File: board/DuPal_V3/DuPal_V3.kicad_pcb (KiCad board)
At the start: 2 copper layers, 116.8 x 73.7 mm, 129 parts, among them J1 ZIF Socket, J2 Debug Header, J3 Extra, K1 G6K-2, Q1 2N3904, SW1 RESET, U1 Pico, U10 74HCT166, U11 74HCT166, U12 74HCT166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

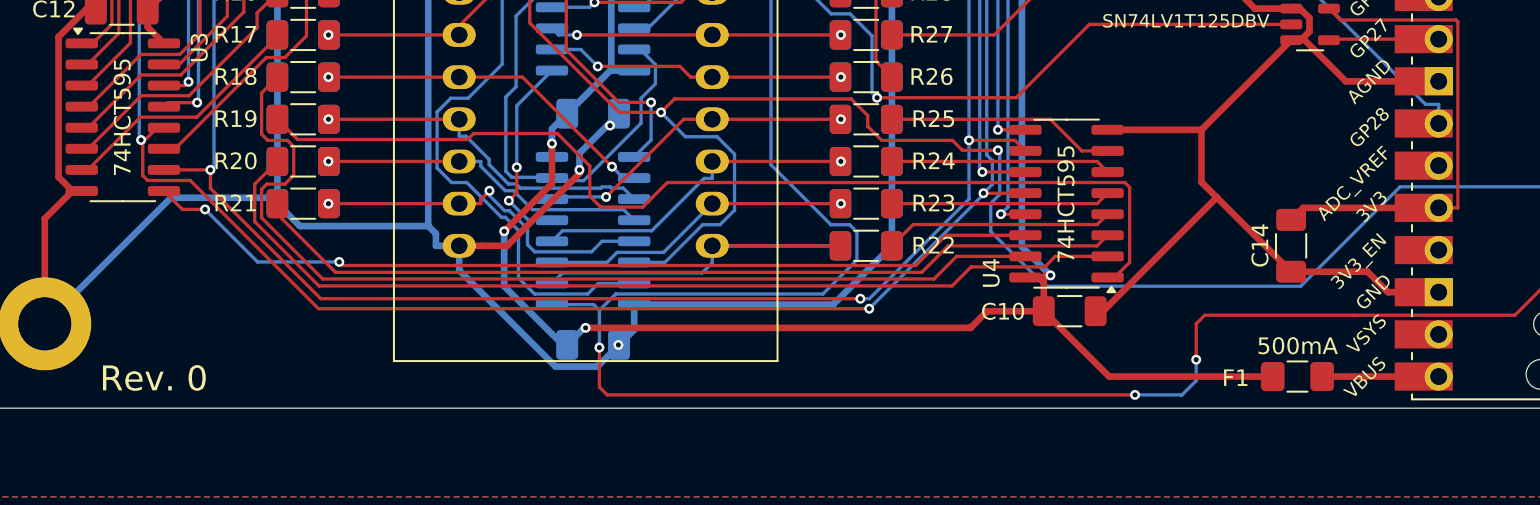
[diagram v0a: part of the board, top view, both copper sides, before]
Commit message: Add external pullup on /RELAY_ENABLE pin to avoid triggering at powerup
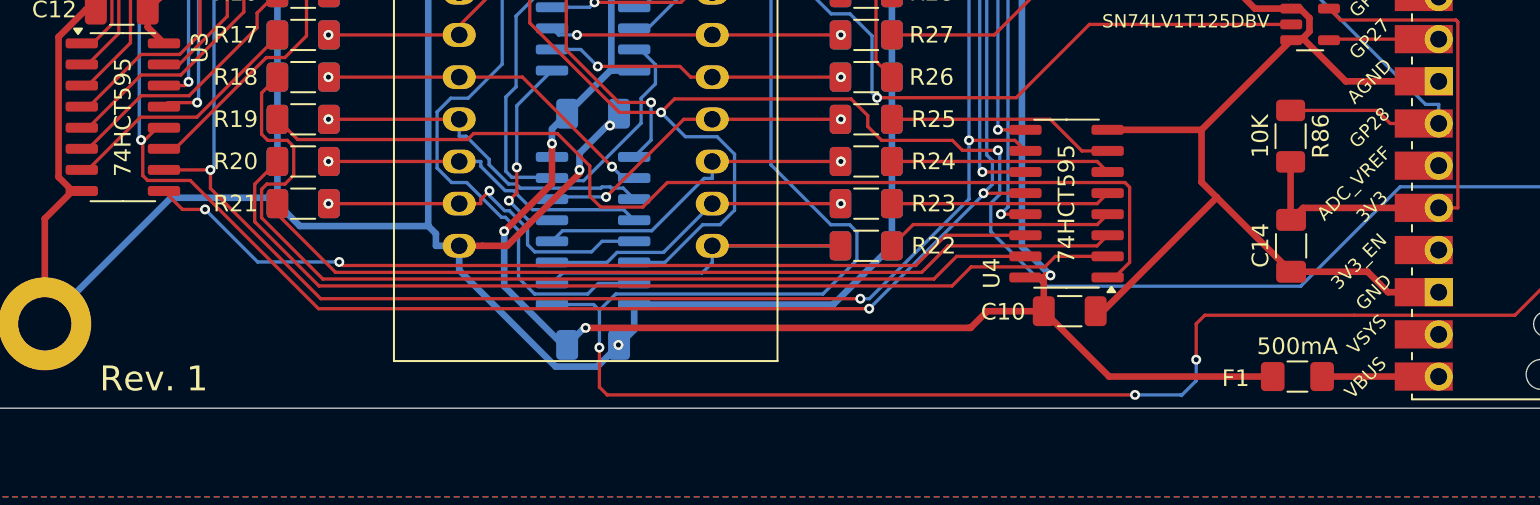
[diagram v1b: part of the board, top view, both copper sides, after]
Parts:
- added R86: 10K, Resistor_SMD:R_1206_3216Metric_Pad1.30x1.75mm_HandSolder, F.Cu at (172.3, 97.9)
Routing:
- net /~{RELAY_ENABLE}: track 46.1 -> 55.4 mm
- net +3V3: track 29.6 -> 33.1 mm
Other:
- board text added: "Rev. 1"
- board text removed: "Rev. 0"
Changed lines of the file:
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@@
 	(footprint "Resistor_SMD:R_1206_3216Metric_Pad1.30x1.75mm_HandSolder"
 		(layer "F.Cu")
+		(at 172.309 97.917 -90)
+		(descr "Resistor SMD 1206 (3216 Metric), square (rectangular) end terminal, IPC_7351 nominal with elongated pad for handsoldering. (Body size source: IPC-SM-782 page 72, https://www.pcb-3d.com/wordpress/wp-content/uploads/ipc-sm-782a_amendment_1_and_2.pdf), generated with kicad-footprint-generator")
+		(tags "resistor handsolder")
+		(property "Reference" "R86"
+			(at 0 -1.82 90)
+			(layer "F.SilkS")
+			(effects
+				(font
+					(size 1 1)
+					(thickness 0.15)
+				)
+			)
+		)
+		(property "Value" "10K"
+			(at 0 1.82 90)
+			(layer "F.SilkS")
+			(effects
+				(font
+					(size 1 1)
+					(thickness 0.15)
+				)
+			)
+		)
+		(property "Footprint" "Resistor_SMD:R_1206_3216Metric_Pad1.30x1.75mm_HandSolder"
+			(at 0 0 -90)
+			(unlocked yes)
+			(layer "F.Fab")
+			(hide yes)
+			(effects
+				(font
+					(size 1.27 1.27)
+					(thickness 0.15)
+				)
+			)
+		)
+		(property "Datasheet" ""
+			(at 0 0 -90)
+			(unlocked yes)
+			(layer "F.Fab")
+			(hide yes)
+			(effects
+				(font
+					(size 1.27 1.27)
+					(thickness 0.15)
+				)
+			)
+		)
+		(property "Description" "Resistor, small symbol"
+			(at 0 0 -90)
+			(unlocked yes)
+			(layer "F.Fab")
+			(hide yes)
+			(effects
+				(font
+					(size 1.27 1.27)
+					(thickness 0.15)
+				)
+			)
+		)
+		(property ki_fp_filters "R_*")
+		(sheetname "Root")
+		(sheetfile "DuPal_V3.kicad_sch")
+		(attr smd)
+		(fp_line
+			(start -0.727064 0.91)
+			(end 0.727064 0.91)
+			(stroke
+				(width 0.12)
+				(type solid)
+			)
+			(layer "F.SilkS")
+		)
+		(fp_line
+			(start -0.727064 -0.91)
+			(end 0.727064 -0.91)
+			(stroke
+				(width 0.12)
+				(type solid)
+			)
+			(layer "F.SilkS")
+		)
+		(fp_line
+			(start -2.45 1.12)
+			(end -2.45 -1.12)
+			(stroke
+				(width 0.05)
+				(type solid)
+			)
+			(layer "F.CrtYd")
+		)
+		(fp_line
+			(start 2.45 1.12)
+			(end -2.45 1.12)
+			(stroke
+				(width 0.05)
+				(type solid)
+			)
+			(layer "F.CrtYd")
+		)
+		(fp_line
+			(start -2.45 -1.12)
+			(end 2.45 -1.12)
+			(stroke
+				(width 0.05)
+				(type solid)
+			)
+			(layer "F.CrtYd")
+		)
+		(fp_line
+			(start 2.45 -1.12)
+			(end 2.45 1.12)
+			(stroke
+				(width 0.05)
+				(type solid)
+			)
+			(layer "F.CrtYd")
+		)
+		(fp_line
+			(start -1.6 0.8)
+			(end -1.6 -0.8)
+			(stroke
+				(width 0.1)
+				(type solid)
+			)
+			(layer "F.Fab")
+		)
+		(fp_line
+			(start 1.6 0.8)
+			(end -1.6 0.8)
+			(stroke
+				(width 0.1)
+				(type solid)
+			)
+			(layer "F.Fab")
+		)
+		(fp_line
+			(start -1.6 -0.8)
+			(end 1.6 -0.8)
+			(stroke
+				(width 0.1)
+				(type solid)
+			)
+			(layer "F.Fab")
+		)
+		(fp_line
+			(start 1.6 -0.8)
+			(end 1.6 0.8)
+			(stroke
+				(width 0.1)
+				(type solid)
+			)
+			(layer "F.Fab")
+		)
+		(fp_text user "${REFERENCE}"
+			(at 0 0 90)
+			(layer "F.Fab")
+			(effects
+				(font
+					(size 0.8 0.8)
+					(thickness 0.12)
+				)
+			)
+		)
+		(pad "1" smd roundrect
+			(at -1.55 0 270)
+			(size 1.3 1.75)
+			(layers "F.Cu" "F.Paste" "F.Mask")
+			(roundrect_rratio 0.192308)
+			(net 127 "/~{RELAY_ENABLE}")
+			(pintype "passive")
+		)
+		(pad "2" smd roundrect
+			(at 1.55 0 270)
+			(size 1.3 1.75)
+			(layers "F.Cu" "F.Paste" "F.Mask")
+			(roundrect_rratio 0.192308)
+			(net 4 "+3V3")
+			(pintype "passive")
+		)
+		(model "${KICAD8_3DMODEL_DIR}/Resistor_SMD.3dshapes/R_1206_3216Metric.wrl"
+			(offset
+				(xyz 0 0 0)
+			)
+			(scale
+				(xyz 1 1 1)
+			)
+			(rotate
+				(xyz 0 0 0)
+			)
+		)
+	)
+	(footprint "Resistor_SMD:R_1206_3216Metric_Pad1.30x1.75mm_HandSolder"
+		(layer "F.Cu")
 		(at 112.841 91.821)
 		(descr "Resistor SMD 1206 (3216 Metric), square (rectangular) end terminal, IPC_7351 nominal with elongated pad for handsoldering. (Body size source: IPC-SM-782 page 72, https://www.pcb-3d.com/wordpress/wp-content/uploads/ipc-sm-782a_amendment_1_and_2.pdf), generated with kicad-footprint-generator")
@@
 		)
 	)
-	(gr_text "Rev. 0"
+	(gr_text "Rev. 1"
 		(at 100.584 113.411 0)
 		(layer "F.SilkS")
@@
 	)
 	(segment
+		(start 172.309 102.9285)
+		(end 172.339 102.9585)
+		(width 0.4)
+		(layer "F.Cu")
+		(net 4)
+	)
+	(segment
+		(start 172.309 99.467)
+		(end 172.309 102.9285)
+		(width 0.4)
+		(layer "F.Cu")
+		(net 4)
+	)
+	(segment
 		(start 153.416 49.276)
 		(end 152.846 49.846)
@@
 	)
 	(segment
+		(start 178.308 97.155)
+		(end 177.52 96.367)
+		(width 0.2)
+		(layer "F.Cu")
+		(net 127)
+	)
+	(segment
+		(start 177.52 96.367)
+		(end 172.309 96.367)
+		(width 0.2)
+		(layer "F.Cu")
+		(net 127)
+	)
+	(segment
 		(start 166.2383 62.4814)
 		(end 166.2383 61.2977)
@@
 		(net 127)
 	)
+	(segment
+		(start 181.229 97.155)
+		(end 178.308 97.155)
+		(width 0.2)
+		(layer "F.Cu")
+		(net 127)
+	)
 	(via
 		(at 166.2383 62.4814)
@@
 		(min_thickness 0.25)
 		(filled_areas_thickness no)
-		(fill yes
+		(fill
 			(thermal_gap 0.5)
 			(thermal_bridge_width 0.5)

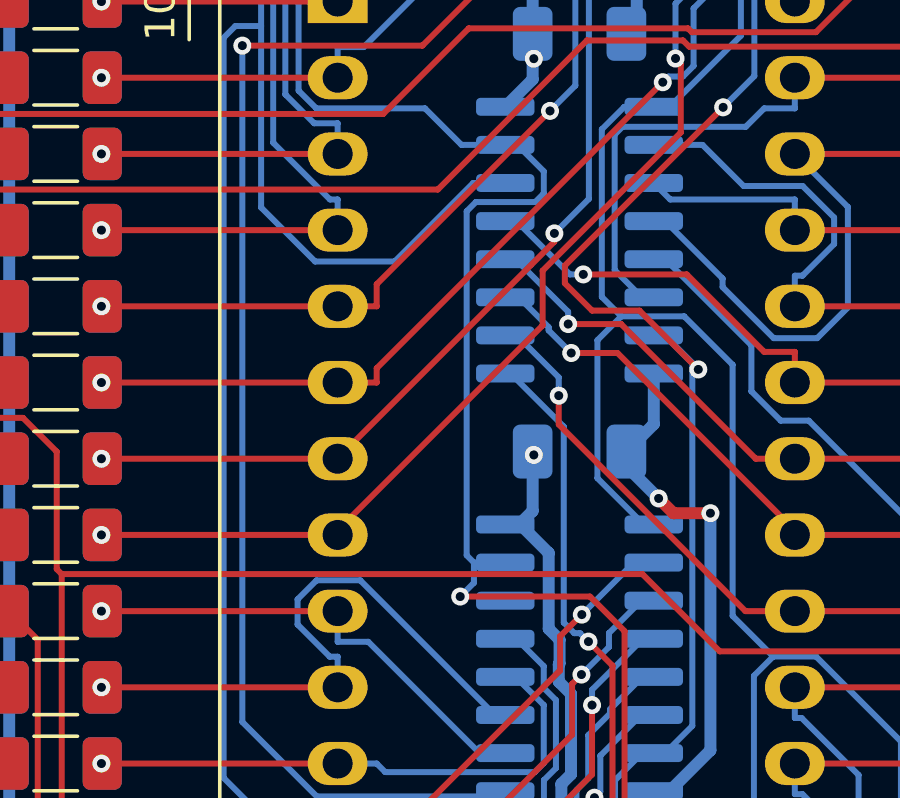
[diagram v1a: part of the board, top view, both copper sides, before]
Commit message: Fix missing connection on a shifter
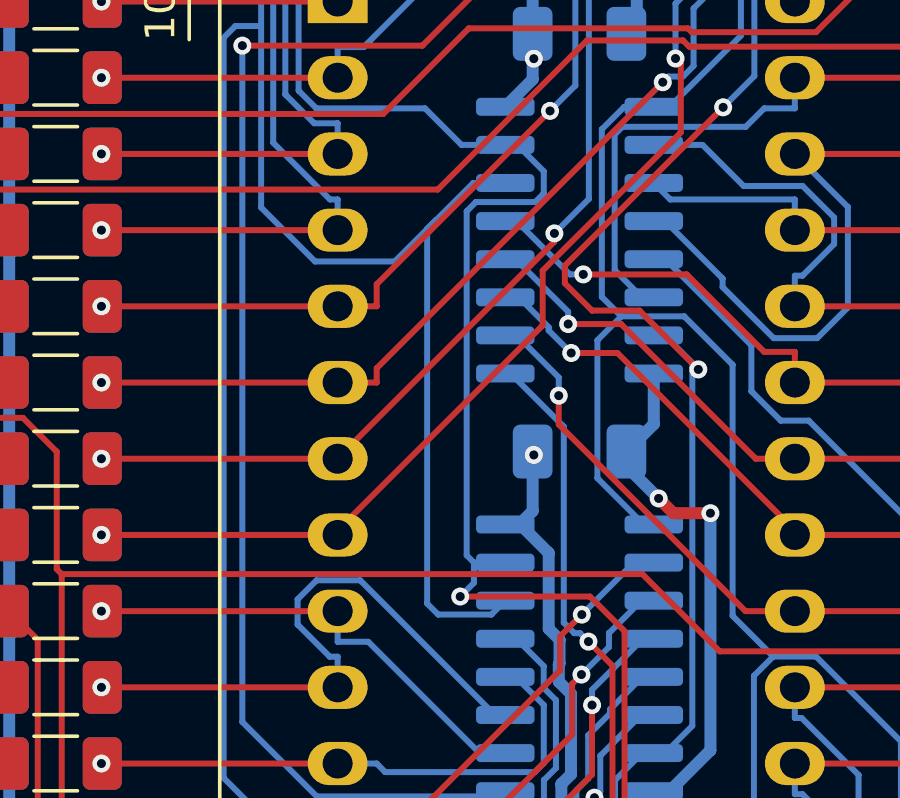
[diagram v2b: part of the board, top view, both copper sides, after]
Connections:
- U9 pad 6: unconnected-(U9-CE-Pad6) -> /PISO_INH
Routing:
- net /PISO_INH: track 178.4 -> 194.3 mm
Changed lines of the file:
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@@
 	(net 139 "Net-(U8-Qh)")
 	(net 140 "Net-(U10-Ds)")
-	(net 141 "unconnected-(U9-CE-Pad6)")
-	(net 142 "Net-(U10-Qh)")
-	(net 143 "Net-(U11-Qh)")
-	(net 144 "/PISO_SER")
+	(net 141 "Net-(U10-Qh)")
+	(net 142 "Net-(U11-Qh)")
+	(net 143 "/PISO_SER")
 	(footprint "Resistor_SMD:R_1206_3216Metric_Pad1.30x1.75mm_HandSolder"
 		(layer "F.Cu")
@@
 			(layers "F.Cu" "F.Paste" "F.Mask")
 			(roundrect_rratio 0.25)
-			(net 144 "/PISO_SER")
+			(net 143 "/PISO_SER")
 			(pinfunction "A")
 			(pintype "input")
@@
 			(layers "B.Cu" "B.Paste" "B.Mask")
 			(roundrect_rratio 0.25)
-			(net 141 "unconnected-(U9-CE-Pad6)")
+			(net 126 "/PISO_INH")
 			(pinfunction "CE")
 			(pintype "input")
@@
 			(layers "B.Cu" "B.Paste" "B.Mask")
 			(roundrect_rratio 0.25)
-			(net 142 "Net-(U10-Qh)")
+			(net 141 "Net-(U10-Qh)")
 			(pinfunction "Ds")
 			(pintype "input")
@@
 			(layers "B.Cu" "B.Paste" "B.Mask")
 			(roundrect_rratio 0.25)
-			(net 143 "Net-(U11-Qh)")
+			(net 142 "Net-(U11-Qh)")
 			(pinfunction "Qh")
 			(pintype "output")
@@
 			(layers "B.Cu" "B.Paste" "B.Mask")
 			(roundrect_rratio 0.25)
-			(net 142 "Net-(U10-Qh)")
+			(net 141 "Net-(U10-Qh)")
 			(pinfunction "Qh")
 			(pintype "output")
@@
 			(layers "B.Cu" "B.Paste" "B.Mask")
 			(roundrect_rratio 0.25)
-			(net 143 "Net-(U11-Qh)")
+			(net 142 "Net-(U11-Qh)")
 			(pinfunction "Ds")
 			(pintype "input")
@@
 			(layers "B.Cu" "B.Paste" "B.Mask")
 			(roundrect_rratio 0.25)
-			(net 144 "/PISO_SER")
+			(net 143 "/PISO_SER")
 			(pinfunction "Qh")
 			(pintype "output")
@@
 	)
 	(segment
+		(start 127.827 73.6928)
+		(end 127.3649 74.1549)
+		(width 0.2)
+		(layer "B.Cu")
+		(net 126)
+	)
+	(segment
 		(start 126.4907 88.2507)
 		(end 127.192 88.2507)
@@
 	)
 	(segment
+		(start 125.5899 74.1549)
+		(end 125.222 73.787)
+		(width 0.2)
+		(layer "B.Cu")
+		(net 126)
+	)
+	(segment
 		(start 119.6886 60.5879)
 		(end 119.6886 54.5378)
@@
 	)
 	(segment
+		(start 125.222 73.787)
+		(end 125.222 61.3058)
+		(width 0.2)
+		(layer "B.Cu")
+		(net 126)
+	)
+	(segment
 		(start 154.7917 98.8768)
 		(end 154.6845 98.7696)
@@
 	)
 	(segment
+		(start 125.222 61.3058)
+		(end 125.5219 61.0059)
+		(width 0.2)
+		(layer "B.Cu")
+		(net 126)
+	)
+	(segment
 		(start 137.7715 97.9494)
 		(end 135.8609 97.9494)
@@
 	)
 	(segment
+		(start 126.7579 59.7699)
+		(end 125.5219 61.0059)
+		(width 0.2)
+		(layer "B.Cu")
+		(net 126)
+	)
+	(segment
 		(start 154.2537 101.9642)
 		(end 154.7917 101.4262)
@@
 	)
 	(segment
-		(start 126.7579 59.7699)
+		(start 125.5219 61.0059)
 		(end 124.1418 62.386)
 		(width 0.2)
@@
 	)
 	(segment
+		(start 127.3649 74.1549)
+		(end 125.5899 74.1549)
+		(width 0.2)
+		(layer "B.Cu")
+		(net 126)
+	)
+	(segment
 		(start 127.192 88.2507)
 		(end 127.827 87.6157)
@@
 		(width 0.2)
 		(layer "F.Cu")
-		(net 142)
+		(net 141)
 	)
 	(segment
@@
 		(width 0.2)
 		(layer "F.Cu")
-		(net 142)
+		(net 141)
 	)
 	(via
@@
 		(drill 0.3)
 		(layers "F.Cu" "B.Cu")
-		(net 142)
+		(net 141)
 	)
 	(via
@@
 		(drill 0.3)
 		(layers "F.Cu" "B.Cu")
-		(net 142)
+		(net 141)
 	)
 	(segment
@@
 		(width 0.2)
 		(layer "B.Cu")
-		(net 142)
+		(net 141)
 	)
 	(segment
@@
 		(width 0.2)
 		(layer "B.Cu")
-		(net 142)
+		(net 141)
 	)
 	(segment
@@
 		(width 0.2)
 		(layer "B.Cu")
-		(net 142)
+		(net 141)
 	)
 	(segment
@@
 		(width 0.2)
 		(layer "B.Cu")
-		(net 142)
+		(net 141)
 	)
 	(segment
@@
 		(width 0.2)
 		(layer "F.Cu")
-		(net 143)
+		(net 142)
 	)
 	(segment
@@
 		(width 0.2)
 		(layer "F.Cu")
-		(net 143)
+		(net 142)
 	)
 	(segment
@@
 		(width 0.2)
 		(layer "F.Cu")
-		(net 143)
+		(net 142)
 	)
 	(segment
@@
 		(width 0.2)
 		(layer "F.Cu")
-		(net 143)
+		(net 142)
 	)
 	(segment
@@
 		(width 0.2)
 		(layer "F.Cu")
-		(net 143)
+		(net 142)
 	)
 	(segment
@@
 		(width 0.2)
 		(layer "F.Cu")
-		(net 143)
+		(net 142)
 	)
 	(via
@@
 		(drill 0.3)
 		(layers "F.Cu" "B.Cu")
-		(net 143)
+		(net 142)
 	)
 	(via
@@
 		(drill 0.3)
 		(layers "F.Cu" "B.Cu")
-		(net 143)
+		(net 142)
 	)
 	(segment
@@
 		(width 0.2)
 		(layer "B.Cu")
-		(net 143)
+		(net 142)
 	)
 	(segment
@@
 		(width 0.2)
 		(layer "B.Cu")
-		(net 143)
+		(net 142)
 	)
 	(segment
@@
 		(width 0.2)
 		(layer "B.Cu")
-		(net 143)
+		(net 142)
 	)
 	(segment
@@
 		(width 0.2)
 		(layer "B.Cu")
-		(net 143)
+		(net 142)
 	)
 	(segment
@@
 		(width 0.2)
 		(layer "B.Cu")
-		(net 143)
+		(net 142)
 	)
 	(segment
@@
 		(width 0.2)
 		(layer "B.Cu")
-		(net 143)
+		(net 142)
 	)
 	(segment
@@
 		(width 0.2)
 		(layer "B.Cu")
-		(net 143)
+		(net 142)
 	)
 	(segment
@@
 		(width 0.2)
 		(layer "B.Cu")
-		(net 143)
+		(net 142)
 	)
 	(segment
@@
 		(width 0.2)
 		(layer "F.Cu")
-		(net 144)
+		(net 143)
 	)
 	(segment
@@
 		(width 0.2)
 		(layer "F.Cu")
-		(net 144)
+		(net 143)
 	)
 	(segment
@@
 		(width 0.2)
 		(layer "F.Cu")
-		(net 144)
+		(net 143)
 	)
 	(via
@@
 		(drill 0.3)
 		(layers "F.Cu" "B.Cu")
-		(net 144)
+		(net 143)
 	)
 	(segment
@@
 		(width 0.2)
 		(layer "B.Cu")
-		(net 144)
+		(net 143)
 	)
 	(segment
@@
 		(width 0.2)
 		(layer "B.Cu")
-		(net 144)
+		(net 143)
 	)
 	(segment
@@
 		(width 0.2)
 		(layer "B.Cu")
-		(net 144)
+		(net 143)
 	)
 	(segment
@@
 		(width 0.2)
 		(layer "B.Cu")
-		(net 144)
+		(net 143)
 	)
 	(segment
@@
 		(width 0.2)
 		(layer "B.Cu")
-		(net 144)
+		(net 143)
 	)
 	(segment
@@
 		(width 0.2)
 		(layer "B.Cu")
-		(net 144)
+		(net 143)
 	)
 	(segment
@@
 		(width 0.2)
 		(layer "B.Cu")
-		(net 144)
+		(net 143)
 	)
 	(segment
@@
 		(width 0.2)
 		(layer "B.Cu")
-		(net 144)
+		(net 143)
 	)
 	(segment
@@
 		(width 0.2)
 		(layer "B.Cu")
-		(net 144)
+		(net 143)
 	)
 	(segment
@@
 		(width 0.2)
 		(layer "B.Cu")
-		(net 144)
+		(net 143)
 	)
 	(segment
@@
 		(width 0.2)
 		(layer "B.Cu")
-		(net 144)
+		(net 143)
 	)
 	(segment
@@
 		(width 0.2)
 		(layer "B.Cu")
-		(net 144)
+		(net 143)
 	)
 	(zone

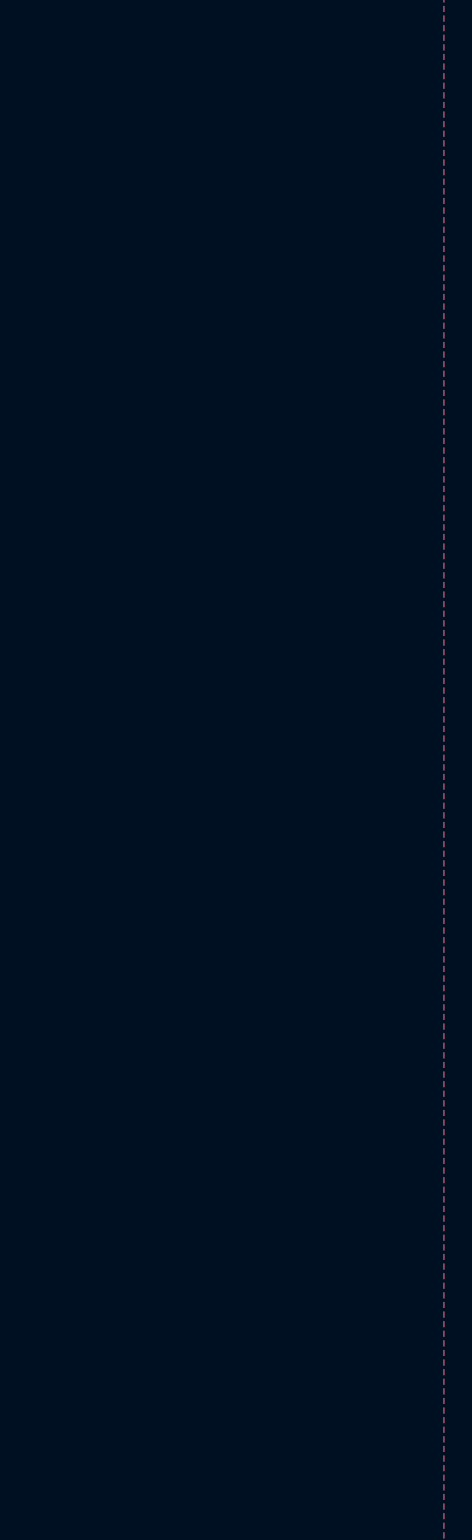
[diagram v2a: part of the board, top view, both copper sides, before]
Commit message: Add pinheaders in schematic
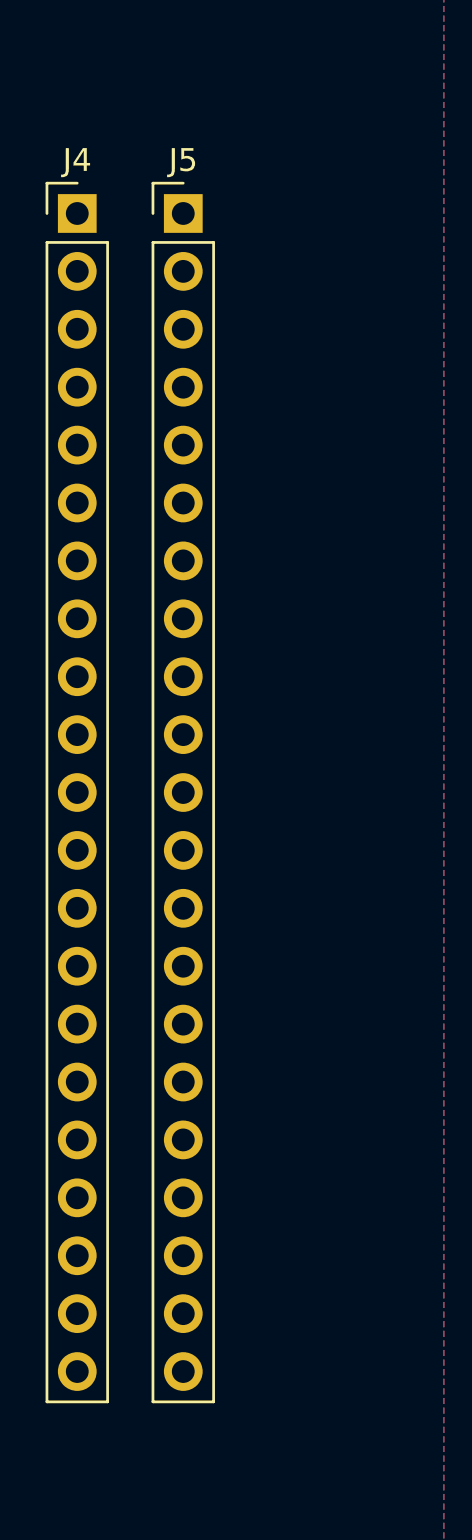
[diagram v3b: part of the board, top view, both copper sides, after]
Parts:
- added J4: Conn_01x21_Pin, Connector_PinHeader_2.54mm:PinHeader_1x21_P2.54mm_Vertical, F.Cu at (72.8, 46.4)
- added J5: Conn_01x21_Pin, Connector_PinHeader_2.54mm:PinHeader_1x21_P2.54mm_Vertical, F.Cu at (77.5, 46.4)
